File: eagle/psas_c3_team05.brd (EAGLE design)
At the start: 76.2 x 71.1 mm, 99 parts, among them IC1 CP2102, J1 3220-10-0100-00, J2 1.27MM_HDR_2X12X1, U1 MIC5319 3.3V, U2 MCP73871, U3 MKW01Z128, X1 32 MHz, X2 32 MHz

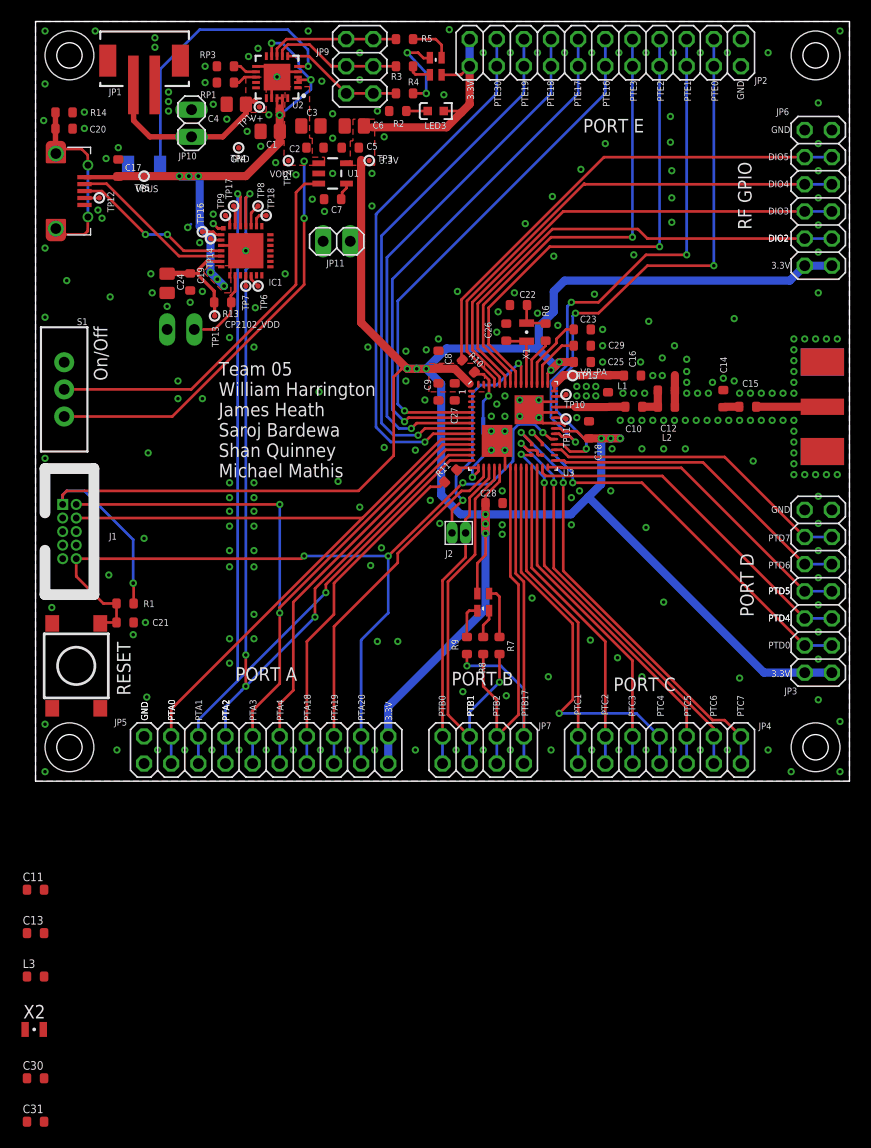
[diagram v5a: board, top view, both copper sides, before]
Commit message: Fixed changed components on the layout
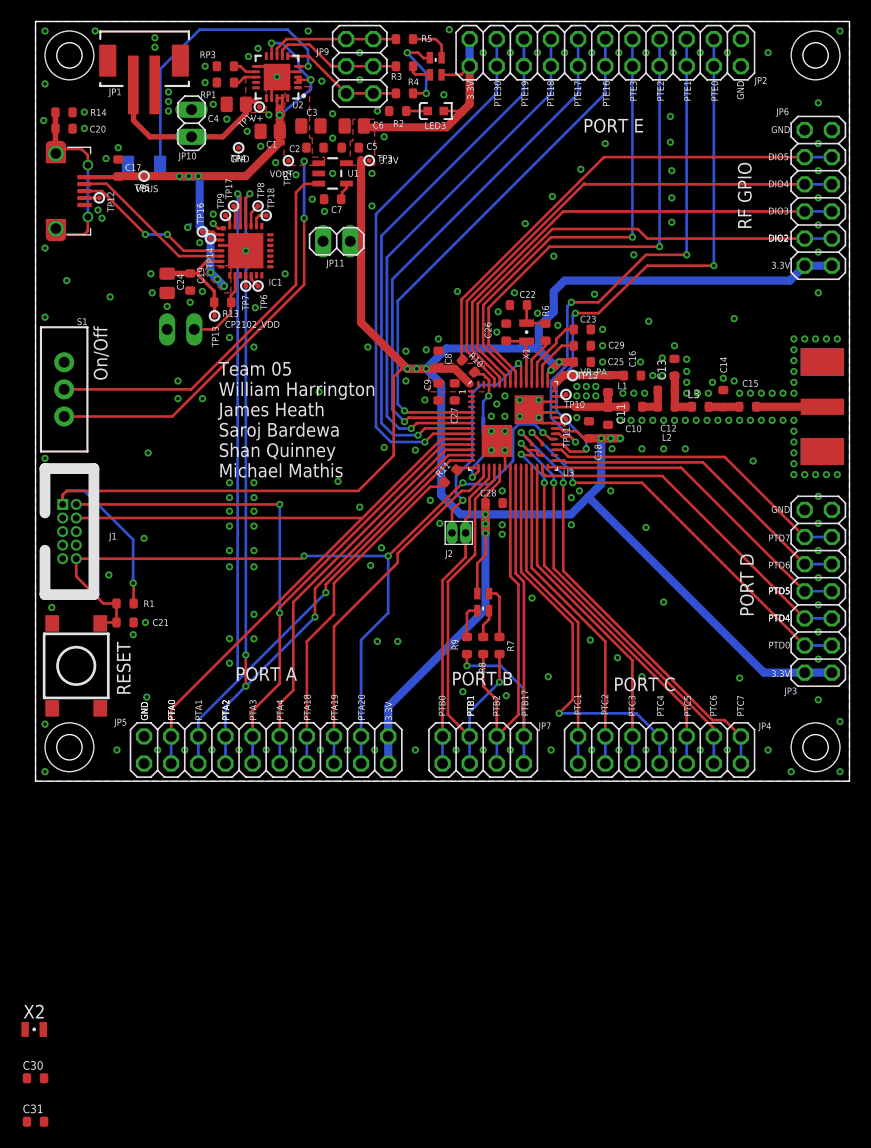
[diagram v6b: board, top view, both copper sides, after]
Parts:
- moved L3 82.0 mm to (62.2, 35.1)
- moved C13 79.9 mm to (59.8, 38.7), turned to 90 degrees
- moved C11 69.5 mm to (53.6, 34.2), turned to 270 degrees
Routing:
- net RFIO: track 6.48 -> 8.21 mm
- net N$17: track 2.97 -> 4.55 mm
- net N$21: track 1.83 -> 3.23 mm
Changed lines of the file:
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@@
 <?xml version="1.0" encoding="utf-8"?>
 <!DOCTYPE eagle SYSTEM "eagle.dtd">
-<eagle version="7.3.0">
+<eagle version="7.4.0">
 <drawing>
 <settings>
@@
 <layer number="17" name="Pads" color="2" fill="1" visible="yes" active="yes"/>
 <layer number="18" name="Vias" color="2" fill="1" visible="yes" active="yes"/>
-<layer number="19" name="Unrouted" color="6" fill="1" visible="no" active="yes"/>
+<layer number="19" name="Unrouted" color="6" fill="1" visible="yes" active="yes"/>
 <layer number="20" name="Dimension" color="15" fill="1" visible="yes" active="yes"/>
 <layer number="21" name="tPlace" color="7" fill="1" visible="yes" active="yes"/>
@@
 <layer number="23" name="tOrigins" color="15" fill="1" visible="no" active="yes"/>
 <layer number="24" name="bOrigins" color="15" fill="1" visible="no" active="yes"/>
-<layer number="25" name="tNames" color="7" fill="1" visible="no" active="yes"/>
-<layer number="26" name="bNames" color="7" fill="1" visible="no" active="yes"/>
-<layer number="27" name="tValues" color="7" fill="1" visible="no" active="yes"/>
-<layer number="28" name="bValues" color="7" fill="1" visible="no" active="yes"/>
+<layer number="25" name="tNames" color="7" fill="1" visible="yes" active="yes"/>
+<layer number="26" name="bNames" color="7" fill="1" visible="yes" active="yes"/>
+<layer number="27" name="tValues" color="7" fill="1" visible="yes" active="yes"/>
+<layer number="28" name="bValues" color="7" fill="1" visible="yes" active="yes"/>
 <layer number="29" name="tStop" color="7" fill="3" visible="yes" active="yes"/>
 <layer number="30" name="bStop" color="7" fill="6" visible="no" active="yes"/>
@@
 <attribute name="VALUE" x="30.734" y="53.721" size="1.27" layer="27" rot="R180"/>
 </element>
-<element name="C11" library="rcl_custom" package=".0603-B-NOSILK" value="12p" x="0" y="-10.16">
-<attribute name="MFG" value="AVX" x="0" y="-10.16" size="1.778" layer="27" display="off"/>
-<attribute name="DIST" value="Mouser" x="0" y="-10.16" size="1.778" layer="27" display="off"/>
-<attribute name="MFG-PN" value="06035A120FAT2A" x="0" y="-10.16" size="1.778" layer="27" display="off"/>
-<attribute name="DPN" value="581-06035A120FAT2A" x="0" y="-10.16" size="1.778" layer="27" display="off"/>
-</element>
-<element name="C13" library="rcl_custom" package=".0603-B-NOSILK" value="15p" x="0" y="-14.224">
-<attribute name="MFG" value="AVX" x="0" y="-14.224" size="1.778" layer="27" display="off"/>
-<attribute name="DIST" value="Digi-Key" x="0" y="-14.224" size="1.778" layer="27" display="off"/>
-<attribute name="MFG-PN" value="06031A150FAT2A" x="0" y="-14.224" size="1.778" layer="27" display="off"/>
-<attribute name="DPN" value="478-6024-1-ND" x="0" y="-14.224" size="1.778" layer="27" display="off"/>
-</element>
-<element name="L3" library="rcl_custom" package=".0603-B-NOSILK" value="15n" x="0" y="-18.288">
-<attribute name="DPN" value="490-6866-1-ND" x="0" y="-18.288" size="1.778" layer="27" display="off"/>
-<attribute name="MFG-PN" value="LQW18AN15NG00D" x="0" y="-18.288" size="1.778" layer="27" display="off"/>
-<attribute name="MFG" value="Murata" x="0" y="-18.288" size="1.778" layer="27" display="off"/>
-<attribute name="DIST" value="Digi-Key" x="0" y="-18.288" size="1.778" layer="27" display="off"/>
+<element name="C11" library="rcl_custom" package=".0603-B-NOSILK" value="12p" x="53.594" y="34.163" rot="R270">
+<attribute name="MFG" value="AVX" x="53.594" y="34.163" size="1.778" layer="27" rot="R270" display="off"/>
+<attribute name="DIST" value="Mouser" x="53.594" y="34.163" size="1.778" layer="27" rot="R270" display="off"/>
+<attribute name="MFG-PN" value="06035A120FAT2A" x="53.594" y="34.163" size="1.778" layer="27" rot="R270" display="off"/>
+<attribute name="DPN" value="581-06035A120FAT2A" x="53.594" y="34.163" size="1.778" layer="27" rot="R270" display="off"/>
+</element>
+<element name="C13" library="rcl_custom" package=".0603-B-NOSILK" value="15p" x="59.817" y="38.735" rot="R90">
+<attribute name="MFG" value="AVX" x="59.817" y="38.735" size="1.778" layer="27" rot="R90" display="off"/>
+<attribute name="DIST" value="Digi-Key" x="59.817" y="38.735" size="1.778" layer="27" rot="R90" display="off"/>
+<attribute name="MFG-PN" value="06031A150FAT2A" x="59.817" y="38.735" size="1.778" layer="27" rot="R90" display="off"/>
+<attribute name="DPN" value="478-6024-1-ND" x="59.817" y="38.735" size="1.778" layer="27" rot="R90" display="off"/>
+</element>
+<element name="L3" library="rcl_custom" package=".0603-B-NOSILK" value="15n" x="62.23" y="35.052">
+<attribute name="DPN" value="490-6866-1-ND" x="62.23" y="35.052" size="1.778" layer="27" display="off"/>
+<attribute name="MFG-PN" value="LQW18AN15NG00D" x="62.23" y="35.052" size="1.778" layer="27" display="off"/>
+<attribute name="MFG" value="Murata" x="62.23" y="35.052" size="1.778" layer="27" display="off"/>
+<attribute name="DIST" value="Digi-Key" x="62.23" y="35.052" size="1.778" layer="27" display="off"/>
 </element>
 <element name="X2" library="crystal" package="FC-12M" value="32 MHz" x="-0.127" y="-23.241">
@@
 <wire x1="18.161" y1="13.335" x2="20.447" y2="13.335" width="0" layer="19" extent="1-1"/>
 <wire x1="18.161" y1="11.049" x2="18.161" y2="13.335" width="0" layer="19" extent="1-1"/>
-<wire x1="0.8" y1="-10.16" x2="0.889" y2="0.889" width="0" layer="19" extent="1-1"/>
-<wire x1="0.8" y1="-14.224" x2="0.8" y2="-10.16" width="0" layer="19" extent="1-1"/>
-<wire x1="0.8" y1="-27.813" x2="0.8" y2="-14.224" width="0" layer="19" extent="1-1"/>
+<wire x1="53.594" y1="33.363" x2="0.889" y2="0.889" width="0" layer="19" extent="1-1"/>
+<wire x1="59.817" y1="39.535" x2="53.594" y2="33.363" width="0" layer="19" extent="1-1"/>
+<wire x1="0.8" y1="-27.813" x2="59.817" y2="39.535" width="0" layer="19" extent="1-1"/>
 <wire x1="0.8" y1="-31.877" x2="0.8" y2="-27.813" width="0" layer="19" extent="1-1"/>
 </signal>
@@
 <contactref element="L1" pad="2"/>
 <wire x1="48.5818" y1="35.024" x2="50.546" y2="35.024" width="0.254" layer="1"/>
-<wire x1="50.546" y1="35.024" x2="53.533" y2="35.024" width="0.762" layer="1"/>
 <wire x1="55.207" y1="35.052" x2="53.683" y2="35.052" width="0.762" layer="1"/>
 <contactref element="C11" pad="1"/>
-<wire x1="53.683" y1="35.052" x2="53.594" y2="36.411" width="0" layer="19" extent="1-1"/>
-<wire x1="53.533" y1="35.024" x2="53.683" y2="35.052" width="0" layer="19" extent="1-1"/>
-<wire x1="-0.8" y1="-10.16" x2="48.5818" y2="35.024" width="0" layer="19" extent="1-1"/>
+<wire x1="53.594" y1="36.411" x2="53.594" y2="35.306" width="0.762" layer="1"/>
+<wire x1="53.594" y1="35.306" x2="53.594" y2="35.141" width="0.762" layer="1"/>
+<wire x1="53.594" y1="35.141" x2="53.683" y2="35.052" width="0.762" layer="1"/>
+<wire x1="53.683" y1="35.052" x2="50.574" y2="35.052" width="0.762" layer="1"/>
+<wire x1="50.574" y1="35.052" x2="50.546" y2="35.024" width="0.762" layer="1"/>
+<wire x1="53.594" y1="34.963" x2="53.594" y2="35.141" width="0.762" layer="1"/>
 </signal>
 <signal name="N$17">
@@
 <contactref element="L2" pad="2"/>
 <wire x1="59.855" y1="36.576" x2="59.855" y2="35.052" width="0.762" layer="1"/>
-<wire x1="59.855" y1="36.576" x2="59.855" y2="38.024" width="0.762" layer="1"/>
 <contactref element="C13" pad="1"/>
 <contactref element="L3" pad="1"/>
-<wire x1="-0.8" y1="-14.224" x2="59.855" y2="35.052" width="0" layer="19" extent="1-1"/>
-<wire x1="-0.8" y1="-18.288" x2="-0.8" y2="-14.224" width="0" layer="19" extent="1-1"/>
+<wire x1="59.855" y1="35.052" x2="61.43" y2="35.052" width="0.762" layer="1"/>
+<wire x1="59.855" y1="38.024" x2="59.817" y2="37.935" width="0" layer="19" extent="1-1"/>
+<wire x1="59.855" y1="38.024" x2="59.855" y2="36.576" width="0.762" layer="1"/>
 </signal>
 <signal name="N$18">
@@
 <wire x1="64.3" y1="34.925" x2="64.389" y2="35.014" width="0.254" layer="1"/>
 <contactref element="L3" pad="2"/>
-<wire x1="0.8" y1="-18.288" x2="64.262" y2="34.925" width="0" layer="19" extent="1-1"/>
+<wire x1="63.03" y1="35.052" x2="64.389" y2="35.052" width="0.762" layer="1"/>
+<wire x1="64.389" y1="35.052" x2="64.389" y2="35.014" width="0.762" layer="1"/>
 </signal>
 <signal name="PTA1">

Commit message: took extra crystal off schematic, corrected bogus airwire
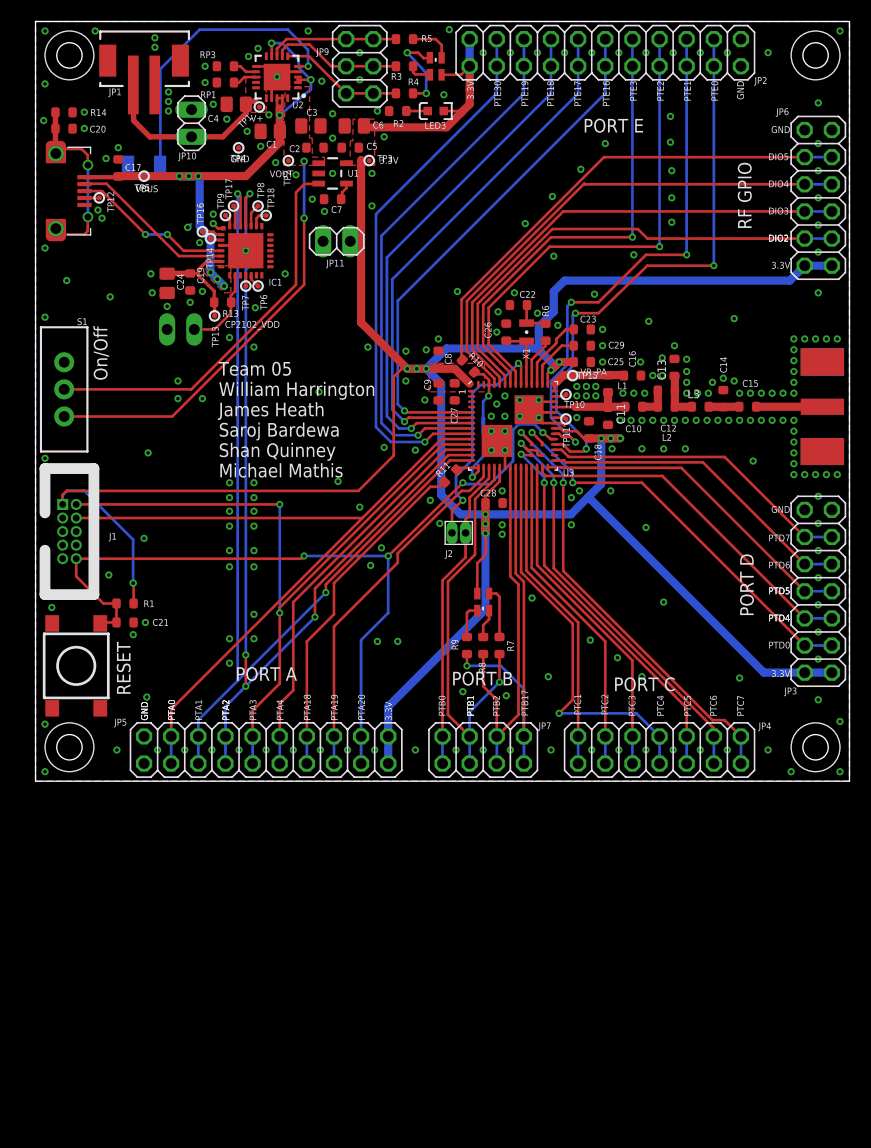
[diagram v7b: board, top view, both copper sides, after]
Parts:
- removed C30, C31: 5pF, Vibrogait_prototype:.0603-B-NOSILK
- removed X2: 32 MHz, crystal:FC-12M
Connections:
- removed net N$14: C31.1, X2.2
- removed net N$16: C30.1, X2.1
- net GND: no longer C30.2, C31.2
